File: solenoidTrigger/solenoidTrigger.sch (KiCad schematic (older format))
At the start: 45 parts, among them J8 CONN_02X03, P1 OSTTC03, P2 OSTTC02, P3 OSTTC08, P4 OSTTC03, P5 OSTTC03, Q1 NMOS_CDS16, Q2 NMOS_CDS16, Q3 NMOS_CDS16, Q4 NMOS_CDS16, Q5 NMOS_CDS16, Q6 NMOS_CDS16, U1 L78M05CDT-TR, U2 ATmega328P-AU, Y2 Crystal_SMD

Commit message: added another LED, changed some pins, changed flybacks
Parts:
- removed D7: SS110LW, footprints:D_SOD-123W_OEM, symbol Rocketry:SS110LW
- removed P3: OSTTC08, footprints:OSTTC080162, symbol Rocketry:OSTTC08
- removed P5: OSTTC03, footprints:OSTTC030162, symbol Rocketry:OSTTC03
- removed Q3, Q6: NMOS_CDS16, footprints:CSD16322Q5, symbol Rocketry:NMOS_CDS16
- removed R4, R7: R_1K, footprints:R_0805_OEM, symbol Rocketry:R_1K
- added D?: LED_0805, footprints:LED_0805_OEM, symbol Rocketry:LED_0805
- added J1: Conn_01x09_Female, Connector_JST:JST_EH_B9B-EH-A_1x09_P2.50mm_Vertical, symbol Connector:Conn_01x09_Female
- added R?: R_499, footprints:R_0805_OEM, symbol Rocketry:R_499
- U2: symbol MCU_Microchip_ATmega:ATmega328P-AU -> solenoidTrigger-rescue:ATmega328P-AU-MCU_Microchip_ATmega
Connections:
- net labels removed: 12V_Solenoid3, ctrl_pin_3-1, ctrl_pin_3-2
- wire segments 95 -> 81
- no-connect marks 9 -> 12
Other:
- moved on the sheet: D3, D4, D5, D6, R11, R12, R13, R14

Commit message: removed switch
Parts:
- removed F2: 01530008Z, footprints:01530008Z, symbol Rocketry:01530008Z
- gave numbers to parts that had none: 2
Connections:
- net 12V_High is gone; now on net 12V_Switch: F3.1
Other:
- note removed: "switch\n"
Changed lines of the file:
@@
 	0    1    1    0
 $EndComp
-Text Label 2850 8100 3    50   ~ 0
-12V_High
-$Comp
-L Rocketry:01530008Z F2
-U 1 1 5DF8F17C
-P 3150 8000
-F 0 "F2" V 2900 7700 50  0000 L CNN
-F 1 "01530008Z" V 3000 7550 50  0000 L CNN
-F 2 "footprints:01530008Z" H 3100 7800 50  0001 C CNN
-F 3 "https://www.littelfuse.com/~/media/commercial-vehicle/datasheets/automotive-fuse-holders/mini/littelfuse_fuse-holders-mini-153-pc-datasheet.pdf" H 3100 7800 50  0001 C CNN
-F 4 "01530008Z" H 3250 8000 50  0001 C CNN "MPN"
-F 5 "F065-ND" H 3250 8000 50  0001 C CNN "DPN"
-F 6 "https://www.digikey.com/product-detail/en/littelfuse-inc/01530008Z/F065-ND/183334" H 3250 8000 50  0001 C CNN "Purchasing Link"
-F 7 "This is just a fuse reciprocal, the fuse it will hold is 0297010.WXNV (https://www.digikey.com/product-detail/en/littelfuse-inc/0297010.WXNV/F991-ND/146591)" H 3250 8000 50  0001 C CNN "Notes"
-	1    3150 8000
-	0    1    1    0
-$EndComp
-Text Label 2950 8100 3    50   ~ 0
-12V_Switch
-Text Notes 2750 7700 0    59   ~ 0
-switch\n
 Text Notes 1850 6700 0    59   ~ 0
 low-power fuse
@@
 Source(12V)
 Text Label 2250 8100 3    50   ~ 0
-12V_High
+12V_Switch
 $Comp
 L Rocketry:01530008Z F3
@@
 NoConn ~ 9600 8600
 $Comp
-L Rocketry:LED_0805 D?
+L Rocketry:LED_0805 D7
 U 1 1 5E369B3B
 P 11850 8150
-F 0 "D?" V 11889 8033 50  0000 R CNN
+F 0 "D7" V 11889 8033 50  0000 R CNN
 F 1 "LED_0805" V 11798 8033 50  0000 R CNN
 F 2 "footprints:LED_0805_OEM" H 11750 8150 50  0001 C CNN
@@
 	11850 8300 11850 8500
 $Comp
-L Rocketry:R_499 R?
+L Rocketry:R_499 R3
 U 1 1 5E369B45
 P 11850 7850
-F 0 "R?" V 12057 7850 50  0000 C CNN
+F 0 "R3" V 12057 7850 50  0000 C CNN
 F 1 "R_499" V 11966 7850 50  0000 C CNN
 F 2 "footprints:R_0805_OEM" H 11780 7850 50  0001 C CNN
@@
 $EndComp
 $Comp
-L power:GND #PWR?
+L power:GND #PWR0103
 U 1 1 5E369B4B
 P 11850 8500
-F 0 "#PWR?" H 11850 8250 50  0001 C CNN
+F 0 "#PWR0103" H 11850 8250 50  0001 C CNN
 F 1 "GND" H 11855 8327 50  0000 C CNN
 F 2 "" H 11850 8500 50  0001 C CNN

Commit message: labeling
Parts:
- renumbered D7 to HFuseLED1, D4 to PLED-1, D5 to PLED-2, D6 to PLED-3, D1 to PowerLED1, D3 to VCCLED1, P2 to battery_conn1, D8 to fly-sol1, D2 to fly-sol2, F3 to high_fuse1, U1 to lin_reg1, F1 to low_fuse1, J8 to prog_conn1, R1 to r_tres1_sol1, R2 to r_tres1_sol2, R5 to r_tres2_sol1, R6 to r_tres2_sol2, J1 to radio_conn1, P1 to sol_conn-1, P4 to sol_conn-2, Q1 to tres1_sol1, Q2 to tres1_sol2, Q4 to tres2_sol1, Q5 to tres2_sol2

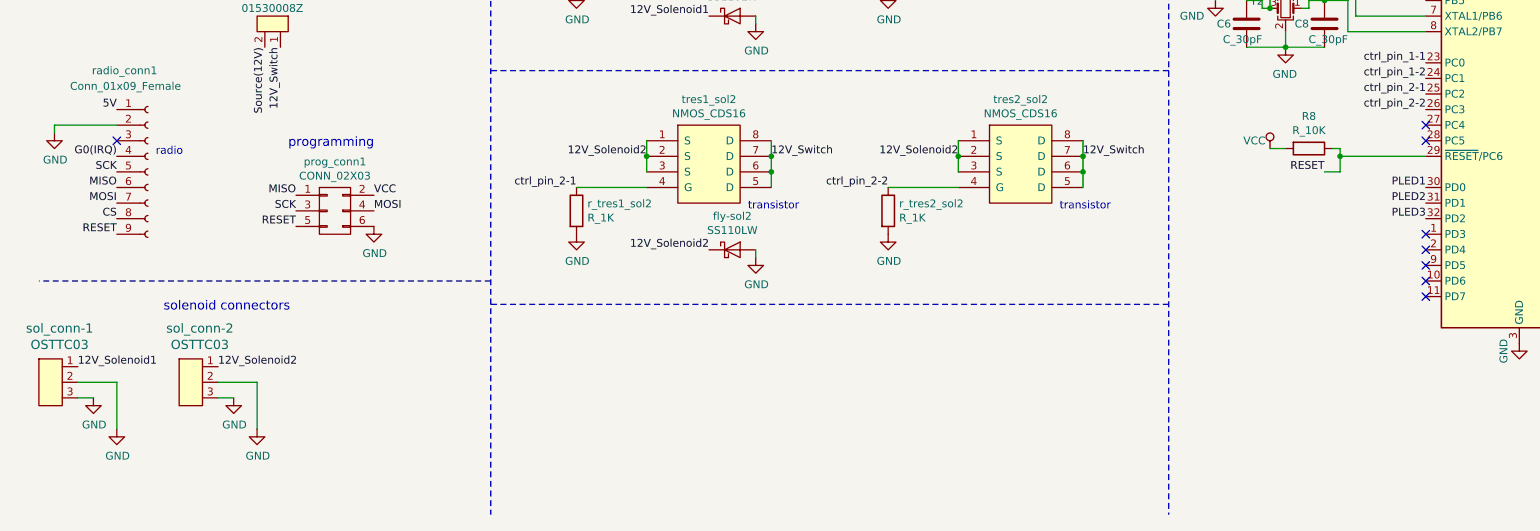
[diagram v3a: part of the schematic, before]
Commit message: added back 3rd solenoid
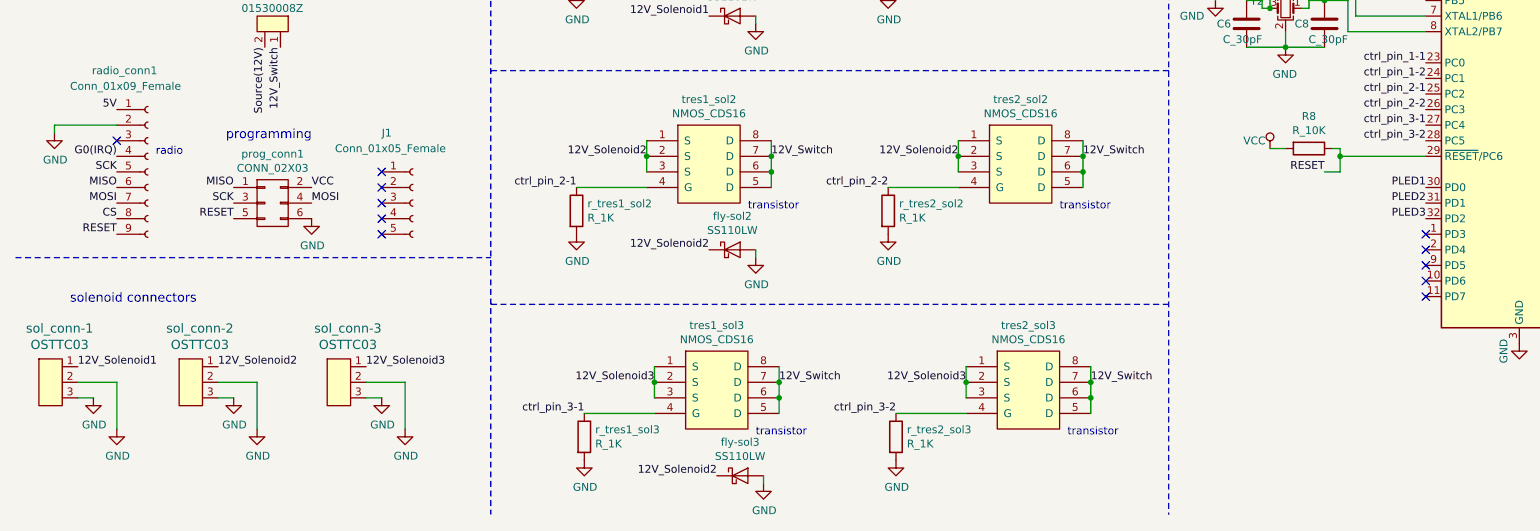
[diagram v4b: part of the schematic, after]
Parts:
- added J1: Conn_01x05_Female, Connector_JST:JST_EH_B5B-EH-A_1x05_P2.50mm_Vertical, symbol Connector:Conn_01x05_Female
- added fly-sol3: SS110LW, footprints:D_SOD-123W_OEM, symbol Rocketry:SS110LW
- added r_tres1_sol3, r_tres2_sol3: R_1K, footprints:R_0805_OEM, symbol Rocketry:R_1K
- added sol_conn-3: OSTTC03, footprints:OSTTC030162, symbol Rocketry:OSTTC03
- added tres1_sol3, tres2_sol3: NMOS_CDS16, footprints:CSD16322Q5, symbol Rocketry:NMOS_CDS16
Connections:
- net 12V_Solenoid2: now also fly-sol3.1 (K)
- net 12V_Switch: now also tres1_sol3.5 (D), tres1_sol3.6 (D), tres1_sol3.7 (D), tres1_sol3.8 (D), tres2_sol3.5 (D), tres2_sol3.6 (D), tres2_sol3.7 (D), tres2_sol3.8 (D)
- net GND: now also fly-sol3.2 (A), r_tres1_sol3.2, r_tres2_sol3.2, sol_conn-3.2, sol_conn-3.3
- net ctrl_pin_3-1: now reaches U2.27 (PC4)
- net ctrl_pin_3-1: now also r_tres1_sol3.1, tres1_sol3.4 (G)
- net ctrl_pin_3-2: now reaches U2.28 (PC5)
- net ctrl_pin_3-2: now also r_tres2_sol3.1, tres2_sol3.4 (G)
- new net 12V_Solenoid3: sol_conn-3.1, tres1_sol3.1 (S), tres1_sol3.2 (S), tres1_sol3.3 (S), tres2_sol3.1 (S), tres2_sol3.2 (S), tres2_sol3.3 (S)
- no-connect marks 12 -> 15
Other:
- moved on the sheet: prog_conn1

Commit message: starting adding fills
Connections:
- net 12V_Solenoid2: no longer fly-sol3.1 (K)
- net 12V_Solenoid3: now also fly-sol3.1 (K)
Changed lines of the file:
@@
 	5350 10850 5350 10900
 Text Label 5050 10850 2    50   ~ 0
-12V_Solenoid2
+12V_Solenoid3
 $Comp
 L Rocketry:SS110LW fly-sol3

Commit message: finished unless i want to add a picture to the board
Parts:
- J1: value Conn_01x05_Female -> NoConnectRadio
- renumbered PowerLED1 to BLED1, fly-sol1 to FlySol1, fly-sol2 to FlySol2, fly-sol3 to FlySol3, HFuseLED1 to HFLED1, high_fuse1 to HFuse1, low_fuse1 to LFuse1, lin_reg1 to LinReg1, battery_conn1 to battery1, prog_conn1 to prog1, r_tres1_sol1 to r_tres1sol1, r_tres1_sol2 to r_tres1sol2, r_tres1_sol3 to r_tres1sol3, r_tres2_sol1 to r_tres2sol1, r_tres2_sol2 to r_tres2sol2, r_tres2_sol3 to r_tres2sol3, radio_conn1 to radio1, sol_conn-1 to sol1, sol_conn-2 to sol2, sol_conn-3 to sol3, tres1_sol1 to tres1sol1, tres1_sol2 to tres1sol2, tres1_sol3 to tres1sol3, tres2_sol1 to tres2sol1, tres2_sol2 to tres2sol2, tres2_sol3 to tres2sol3
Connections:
- net ctrl_pin_1-1: no longer r_tres1sol1.1, tres1sol1.4 (G)
- net ctrl_pin_1-2: no longer r_tres2sol1.1, tres2sol1.4 (G)
- net ctrl_pin_2-1: no longer r_tres1sol2.1, tres1sol2.4 (G)
- net ctrl_pin_2-2: no longer r_tres2sol2.1, tres2sol2.4 (G)
- net ctrl_pin_3-1: no longer r_tres1sol3.1, tres1sol3.4 (G)
- net ctrl_pin_3-2: no longer r_tres2sol3.1, tres2sol3.4 (G)
- new net CtrlPin1-1: r_tres1sol1.1, tres1sol1.4 (G)
- new net CtrlPin1-2: r_tres2sol1.1, tres2sol1.4 (G)
- new net CtrlPin2-1: r_tres1sol2.1, tres1sol2.4 (G)
- new net CtrlPin2-2: r_tres2sol2.1, tres2sol2.4 (G)
- new net CtrlPin3-1: r_tres1sol3.1, tres1sol3.4 (G)
- new net CtrlPin3-2: r_tres2sol3.1, tres2sol3.4 (G)
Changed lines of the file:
@@
 Text Label 1200 9100 2    50   ~ 0
 MOSI
-$Comp
-L Rocketry:CONN_02X03 prog_conn1
-U 1 1 5DE2F9C4
-P 2200 9100
-F 0 "prog_conn1" H 2200 9415 50  0000 C CNN
-F 1 "CONN_02X03" H 2200 9324 50  0000 C CNN
-F 2 "footprints:Pin_Header_Straight_2x03" H 2200 7900 50  0001 C CNN
-F 3 "http://portal.fciconnect.com/Comergent//fci/drawing/67996.pdf" H 2200 7900 50  0001 C CNN
-F 4 "DK" H 2200 9100 60  0001 C CNN "MFN"
-F 5 "609-3234-ND" H 2200 9100 60  0001 C CNN "MPN"
-F 6 "https://www.digikey.com/product-detail/en/amphenol-fci/67997-206HLF/609-3234-ND/1878491" H 2600 9700 60  0001 C CNN "PurchasingLink"
-	1    2200 9100
-	1    0    0    -1
-$EndComp
 Wire Wire Line
 	8450 7100 8600 7100
@@
 PLED3
 Text Label 4150 7450 2    50   ~ 0
-ctrl_pin_1-1
+CtrlPin1-1
 Wire Wire Line
 	4600 7150 4600 7250
@@
 transistor
 Text Label 6150 9000 2    50   ~ 0
-ctrl_pin_2-2
+CtrlPin2-2
 $Comp
-L Rocketry:NMOS_CDS16 tres2_sol2
+L Rocketry:NMOS_CDS16 tres2sol2
 U 1 1 5DFB08F5
 P 7000 8700
-F 0 "tres2_sol2" H 7000 8965 50  0000 C CNN
+F 0 "tres2sol2" H 7000 8965 50  0000 C CNN
 F 1 "NMOS_CDS16" H 7000 8874 50  0000 C CNN
 F 2 "footprints:CSD16322Q5" H 6200 8900 50  0001 C CNN
@@
 transistor
 Text Label 6150 7450 2    50   ~ 0
-ctrl_pin_1-2
+CtrlPin1-2
 Wire Wire Line
 	6600 7150 6600 7250
@@
 	4600 8700 4600 8800
 $Comp
-L Rocketry:NMOS_CDS16 tres1_sol2
+L Rocketry:NMOS_CDS16 tres1sol2
 U 1 1 5DCE65D8
 P 5000 8700
-F 0 "tres1_sol2" H 5000 8965 50  0000 C CNN
+F 0 "tres1sol2" H 5000 8965 50  0000 C CNN
 F 1 "NMOS_CDS16" H 5000 8874 50  0000 C CNN
 F 2 "footprints:CSD16322Q5" H 4200 8900 50  0001 C CNN
@@
 $EndComp
 Text Label 4150 9000 2    50   ~ 0
-ctrl_pin_2-1
+CtrlPin2-1
 $Comp
 L power:GND #PWR0131
@@
 $EndComp
 $Comp
-L Regulator_Linear:AMS1117-5.0 lin_reg1
+L Regulator_Linear:AMS1117-5.0 LinReg1
 U 1 1 5DDA38F2
 P 2100 5800
-F 0 "lin_reg1" H 2100 6042 50  0000 C CNN
+F 0 "LinReg1" H 2100 6042 50  0000 C CNN
 F 1 "L78M05CDT-TR " H 2100 5951 50  0000 C CNN
 F 2 "footprints:L78M05CDT-TR" H 2100 6000 50  0001 C CNN
@@
 	7950 6650 7950 11100
 $Comp
-L Rocketry:OSTTC03 sol_conn-1
+L Rocketry:OSTTC03 sol1
 U 1 1 5DE79A1A
 P 850 10000
-F 0 "sol_conn-1" H 833 10096 59  0000 C CNN
+F 0 "sol1" H 833 10096 59  0000 C CNN
 F 1 "OSTTC03" H 833 9991 59  0000 C CNN
 F 2 "footprints:OSTTC030162" H 750 9850 59  0001 C CNN
@@
 $EndComp
 $Comp
-L Rocketry:OSTTC03 sol_conn-2
+L Rocketry:OSTTC03 sol2
 U 1 1 5DE7F97A
 P 1750 10000
-F 0 "sol_conn-2" H 1733 10096 59  0000 C CNN
+F 0 "sol2" H 1733 10096 59  0000 C CNN
 F 1 "OSTTC03" H 1733 9991 59  0000 C CNN
 F 2 "footprints:OSTTC030162" H 1650 9850 59  0001 C CNN
@@
 12V_Low
 $Comp
-L Rocketry:01530008Z low_fuse1
+L Rocketry:01530008Z LFuse1
 U 1 1 5DF76EC6
 P 2450 7000
-F 0 "low_fuse1" V 2200 6700 50  0000 C CNN
+F 0 "LFuse1" V 2200 6700 50  0000 C CNN
 F 1 "01530008Z" V 2300 6550 50  0000 L CNN
 F 2 "footprints:01530008Z" H 2400 6800 50  0001 C CNN
@@
 seems resolved, the pinout in the atmega datasheet is correct\n
 $Comp
-L Rocketry:SS110LW fly-sol1
+L Rocketry:SS110LW FlySol1
 U 1 1 5E107C0A
 P 5150 7900
-F 0 "fly-sol1" H 5150 8116 50  0000 C CNN
+F 0 "FlySol1" H 5150 8116 50  0000 C CNN
 F 1 "SS110LW" H 5150 8025 50  0000 C CNN
 F 2 "footprints:D_SOD-123W_OEM" H 5050 7900 50  0001 C CNN
@@
 12V_Switch
 $Comp
-L Rocketry:01530008Z high_fuse1
+L Rocketry:01530008Z HFuse1
 U 1 1 5E268060
 P 2450 8000
-F 0 "high_fuse1" V 2200 7700 50  0000 C CNN
+F 0 "HFuse1" V 2200 7700 50  0000 C CNN
 F 1 "01530008Z" V 2300 7550 50  0000 L CNN
 F 2 "footprints:01530008Z" H 2400 7800 50  0001 C CNN
@@
 12V_Solenoid2
 $Comp
-L Rocketry:SS110LW fly-sol2
+L Rocketry:SS110LW FlySol2
 U 1 1 5E16DBBE
 P 5150 9400
-F 0 "fly-sol2" H 5150 9616 50  0000 C CNN
+F 0 "FlySol2" H 5150 9616 50  0000 C CNN
 F 1 "SS110LW" H 5150 9525 50  0000 C CNN
 F 2 "footprints:D_SOD-123W_OEM" H 5050 9400 50  0001 C CNN
@@
 	800  8600 1200 8600
 $Comp
-L Connector:Conn_01x09_Female radio_conn1
+L Connector:Conn_01x09_Female radio1
 U 1 1 5E31E4D8
 P 1400 8900
-F 0 "radio_conn1" H 1250 9550 50  0000 C CNN
+F 0 "radio1" H 1250 9550 50  0000 C CNN
 F 1 "Conn_01x09_Female" H 900 9450 50  0000 L CNN
 F 2 "Connector_JST:JST_EH_B9B-EH-A_1x09_P2.50mm_Vertical" H 1400 8900 50  0001 C CNN
@@
 12V_Switch
 $Comp
-L Rocketry:NMOS_CDS16 tres2_sol1
+L Rocketry:NMOS_CDS16 tres2sol1
 U 1 1 5DFB091C
 P 7000 7150
-F 0 "tres2_sol1" H 7000 7415 50  0000 C CNN
+F 0 "tres2sol1" H 7000 7415 50  0000 C CNN
 F 1 "NMOS_CDS16" H 7000 7324 50  0000 C CNN
 F 2 "footprints:CSD16322Q5" H 6200 7350 50  0001 C CNN
@@
 $EndComp
 $Comp
-L Rocketry:NMOS_CDS16 tres1_sol1
+L Rocketry:NMOS_CDS16 tres1sol1
 U 1 1 5DF7F358
 P 5000 7150
-F 0 "tres1_sol1" H 5000 7415 50  0000 C CNN
+F 0 "tres1sol1" H 5000 7415 50  0000 C CNN
 F 1 "NMOS_CDS16" H 5000 7324 50  0000 C CNN
 F 2 "footprints:CSD16322Q5" H 4200 7350 50  0001 C CNN
@@
 $EndComp
 $Comp
-L Rocketry:LED_0805 HFuseLED1
+L Rocketry:LED_0805 HFLED1
 U 1 1 5E369B3B
 P 11850 8150
-F 0 "HFuseLED1" V 11889 8033 50  0000 R CNN
+F 0 "HFLED1" V 11889 8033 50  0000 R CNN
 F 1 "LED_0805" V 11798 8033 50  0000 R CNN
 F 2 "footprints:LED_0805_OEM" H 11750 8150 50  0001 C CNN
@@
 $EndComp
 $Comp
-L Rocketry:OSTTC02 battery_conn1
+L Rocketry:OSTTC02 battery1
 U 1 1 5DEBC83F
 P 1250 7250
-F 0 "battery_conn1" H 1233 7346 59  0000 C CNN
+F 0 "battery1" H 1233 7346 59  0000 C CNN
 F 1 "OSTTC02" H 1233 7241 59  0000 C CNN
 F 2 "footprints:OSTTC02" H 1150 7100 59  0001 C CNN
@@
 $EndComp
 $Comp
-L Rocketry:R_1K r_tres1_sol1
+L Rocketry:R_1K r_tres1sol1
 U 1 1 5DF7F370
 P 4150 7600
-F 0 "r_tres1_sol1" H 4220 7646 50  0000 L CNN
+F 0 "r_tres1sol1" H 4220 7646 50  0000 L CNN
 F 1 "R_1K" H 4220 7555 50  0000 L CNN
 F 2 "footprints:R_0805_OEM" H 4080 7600 50  0001 C CNN
@@
 $EndComp
 $Comp
-L Rocketry:R_1K r_tres2_sol1
+L Rocketry:R_1K r_tres2sol1
 U 1 1 5DFB0934
 P 6150 7600
-F 0 "r_tres2_sol1" H 6220 7646 50  0000 L CNN
+F 0 "r_tres2sol1" H 6220 7646 50  0000 L CNN
 F 1 "R_1K" H 6220 7555 50  0000 L CNN
 F 2 "footprints:R_0805_OEM" H 6080 7600 50  0001 C CNN
@@
 $EndComp
 $Comp
-L Rocketry:R_1K r_tres1_sol2
+L Rocketry:R_1K r_tres1sol2
 U 1 1 5DCE65F0
 P 4150 9150
-F 0 "r_tres1_sol2" H 4220 9196 50  0000 L CNN
+F 0 "r_tres1sol2" H 4220 9196 50  0000 L CNN
 F 1 "R_1K" H 4220 9105 50  0000 L CNN
 F 2 "footprints:R_0805_OEM" H 4080 9150 50  0001 C CNN
@@
 $EndComp
 $Comp
-L Rocketry:R_1K r_tres2_sol2
+L Rocketry:R_1K r_tres2sol2
 U 1 1 5DFB090D
 P 6150 9150
-F 0 "r_tres2_sol2" H 6220 9196 50  0000 L CNN
+F 0 "r_tres2sol2" H 6220 9196 50  0000 L CNN
 F 1 "R_1K" H 6220 9105 50  0000 L CNN
 F 2 "footprints:R_0805_OEM" H 6080 9150 50  0001 C CNN
@@
 $EndComp
 $Comp
-L Rocketry:LED_0805 PowerLED1
+L Rocketry:LED_0805 BLED1
 U 1 1 5DDDFF17
 P 11250 8150
-F 0 "PowerLED1" V 11289 8033 50  0000 R CNN
+F 0 "BLED1" V 11289 8033 50  0000 R CNN
 F 1 "LED_0805" V 11198 8033 50  0000 R CNN
 F 2 "footprints:LED_0805_OEM" H 11150 8150 50  0001 C CNN
@@
 P 3100 9100
 F 0 "J1" H 2900 9550 50  0000 L CNN
-F 1 "Conn_01x05_Female" H 2600 9450 50  0000 L CNN
+F 1 "NoConnectRadio" H 2600 9450 50  0000 L CNN
 F 2 "Connector_JST:JST_EH_B5B-EH-A_1x05_P2.50mm_Vertical" H 3100 9100 50  0001 C CNN
 F 3 "~" H 3100 9100 50  0001 C CNN
@@
 NoConn ~ 2900 9300
 Text Label 6200 10450 2    50   ~ 0
-ctrl_pin_3-2
+CtrlPin3-2
 $Comp
-L Rocketry:NMOS_CDS16 tres2_sol3
+L Rocketry:NMOS_CDS16 tres2sol3
 U 1 1 5E3D3909
 P 7050 10150
-F 0 "tres2_sol3" H 7050 10415 50  0000 C CNN
+F 0 "tres2sol3" H 7050 10415 50  0000 C CNN
 F 1 "NMOS_CDS16" H 7050 10324 50  0000 C CNN
 F 2 "footprints:CSD16322Q5" H 6250 10350 50  0001 C CNN
@@
 	4650 10150 4650 10250
 $Comp
-L Rocketry:NMOS_CDS16 tres1_sol3
+L Rocketry:NMOS_CDS16 tres1sol3
 U 1 1 5E3D3934
 P 5050 10150
-F 0 "tres1_sol3" H 5050 10415 50  0000 C CNN
+F 0 "tres1sol3" H 5050 10415 50  0000 C CNN
 F 1 "NMOS_CDS16" H 5050 10324 50  0000 C CNN
 F 2 "footprints:CSD16322Q5" H 4250 10350 50  0001 C CNN
@@
 $EndComp
 Text Label 4200 10450 2    50   ~ 0
-ctrl_pin_3-1
+CtrlPin3-1
 Text Label 5450 10250 0    50   ~ 0
 12V_Switch
@@
 12V_Solenoid3
 $Comp
-L Rocketry:SS110LW fly-sol3
+L Rocketry:SS110LW FlySol3
 U 1 1 5E3D3948
 P 5200 10850
-F 0 "fly-sol3" H 5200 11066 50  0000 C CNN
+F 0 "FlySol3" H 5200 11066 50  0000 C CNN
 F 1 "SS110LW" H 5200 10975 50  0000 C CNN
 F 2 "footprints:D_SOD-123W_OEM" H 5100 10850 50  0001 C CNN
@@
 $EndComp
 $Comp
-L Rocketry:R_1K r_tres1_sol3
+L Rocketry:R_1K r_tres1sol3
 U 1 1 5E3D3951
 P 4200 10600
-F 0 "r_tres1_sol3" H 4270 10646 50  0000 L CNN
+F 0 "r_tres1sol3" H 4270 10646 50  0000 L CNN
 F 1 "R_1K" H 4270 10555 50  0000 L CNN
 F 2 "footprints:R_0805_OEM" H 4130 10600 50  0001 C CNN
@@
 $EndComp
 $Comp
-L Rocketry:R_1K r_tres2_sol3
+L Rocketry:R_1K r_tres2sol3
 U 1 1 5E3D395A
 P 6200 10600
-F 0 "r_tres2_sol3" H 6270 10646 50  0000 L CNN
+F 0 "r_tres2sol3" H 6270 10646 50  0000 L CNN
 F 1 "R_1K" H 6270 10555 50  0000 L CNN
 F 2 "footprints:R_0805_OEM" H 6130 10600 50  0001 C CNN
@@
 12V_Solenoid3
 $Comp
-L Rocketry:OSTTC03 sol_conn-3
+L Rocketry:OSTTC03 sol3
 U 1 1 5E400A37
 P 2700 10000
-F 0 "sol_conn-3" H 2683 10096 59  0000 C CNN
+F 0 "sol3" H 2683 10096 59  0000 C CNN
 F 1 "OSTTC03" H 2683 9991 59  0000 C CNN
 F 2 "footprints:OSTTC030162" H 2600 9850 59  0001 C CNN
@@
 Text Label 9600 8700 2    50   ~ 0
 ctrl_pin_3-2
+$Comp
+L Rocketry:CONN_02X03 prog1
+U 1 1 5DE2F9C4
+P 2200 9100
+F 0 "prog1" H 2200 9415 50  0000 C CNN
+F 1 "CONN_02X03" H 2200 9324 50  0000 C CNN
+F 2 "footprints:Pin_Header_Straight_2x03" H 2200 7900 50  0001 C CNN
+F 3 "http://portal.fciconnect.com/Comergent//fci/drawing/67996.pdf" H 2200 7900 50  0001 C CNN
+F 4 "DK" H 2200 9100 60  0001 C CNN "MFN"
+F 5 "609-3234-ND" H 2200 9100 60  0001 C CNN "MPN"
+F 6 "https://www.digikey.com/product-detail/en/amphenol-fci/67997-206HLF/609-3234-ND/1878491" H 2600 9700 60  0001 C CNN "PurchasingLink"
+	1    2200 9100
+	1    0    0    -1
+$EndComp
 $EndSCHEMATC
